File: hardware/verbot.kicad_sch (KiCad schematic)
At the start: 7 parts, among them J1 Raspberry Pi Zero 2 W, J2 5V USB power bank, M1 Pimoroni OnOff SHIM, M2 DRV8833 carrier, M3 Verbot 3V motor, M4 Verbot gearbox harness

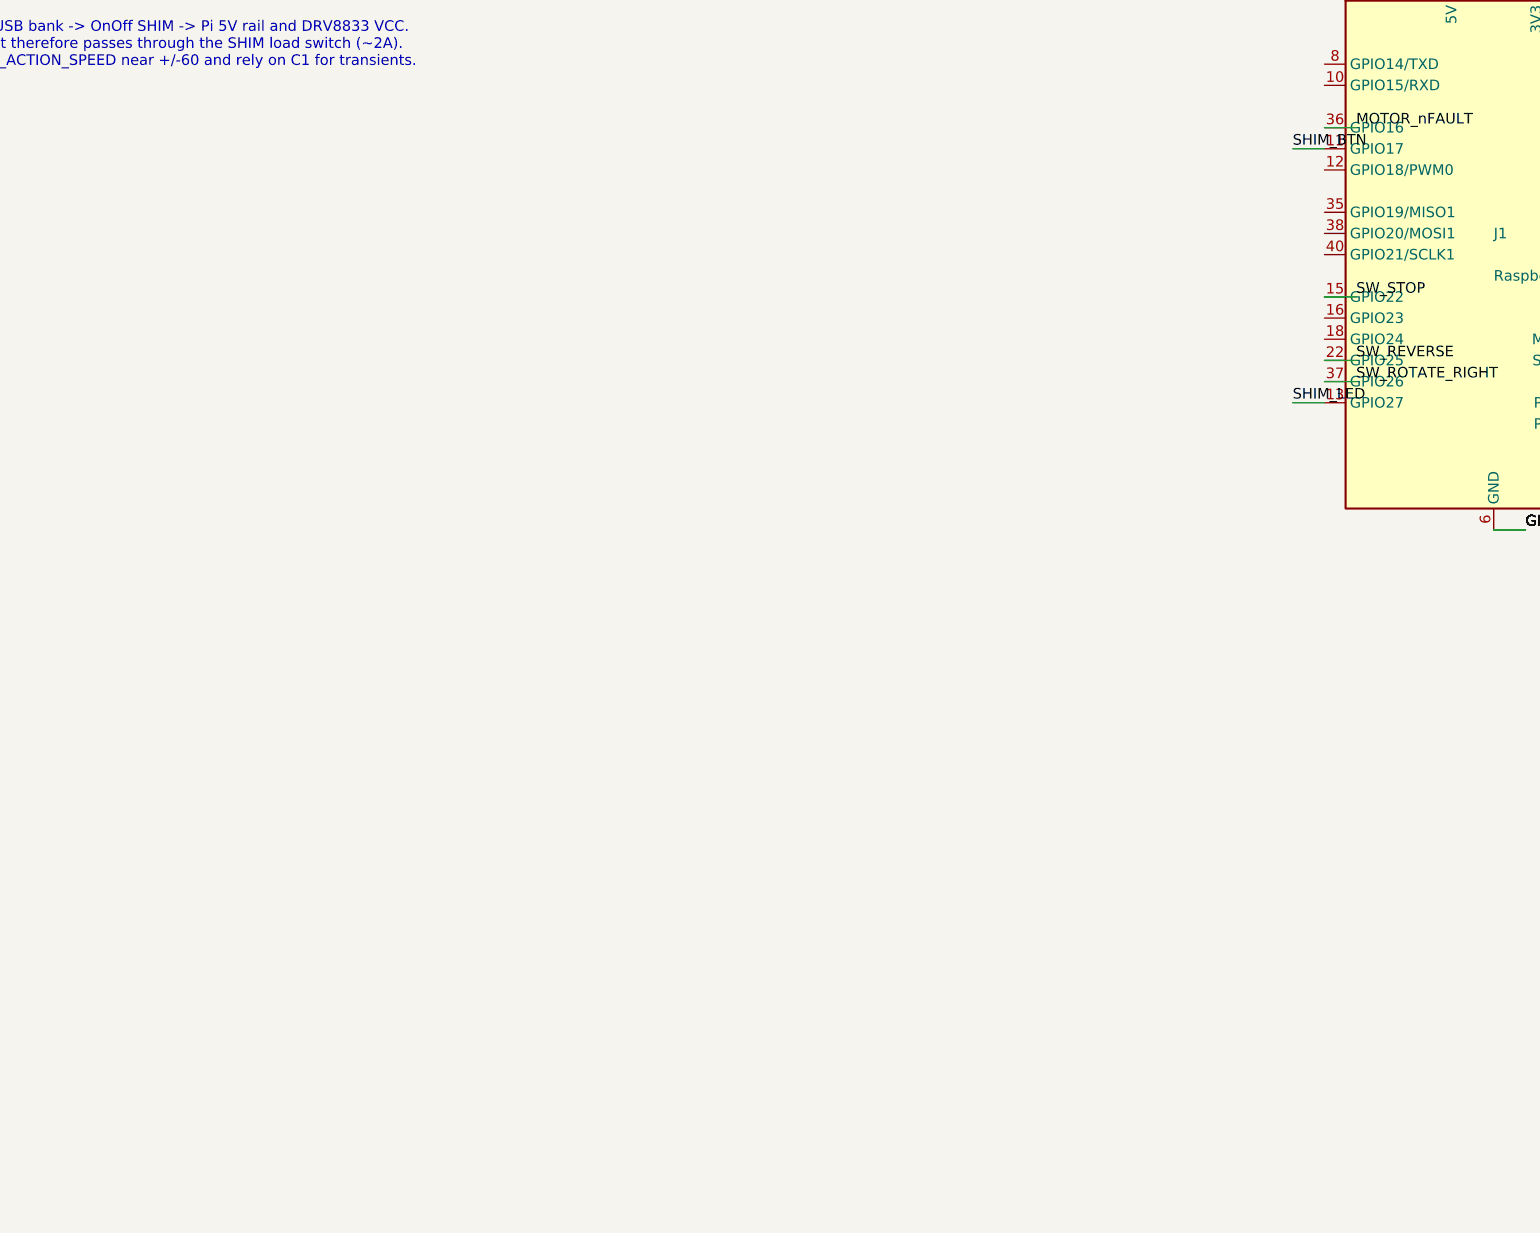
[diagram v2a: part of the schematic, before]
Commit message: feat(hardware): MAX98357A audio section
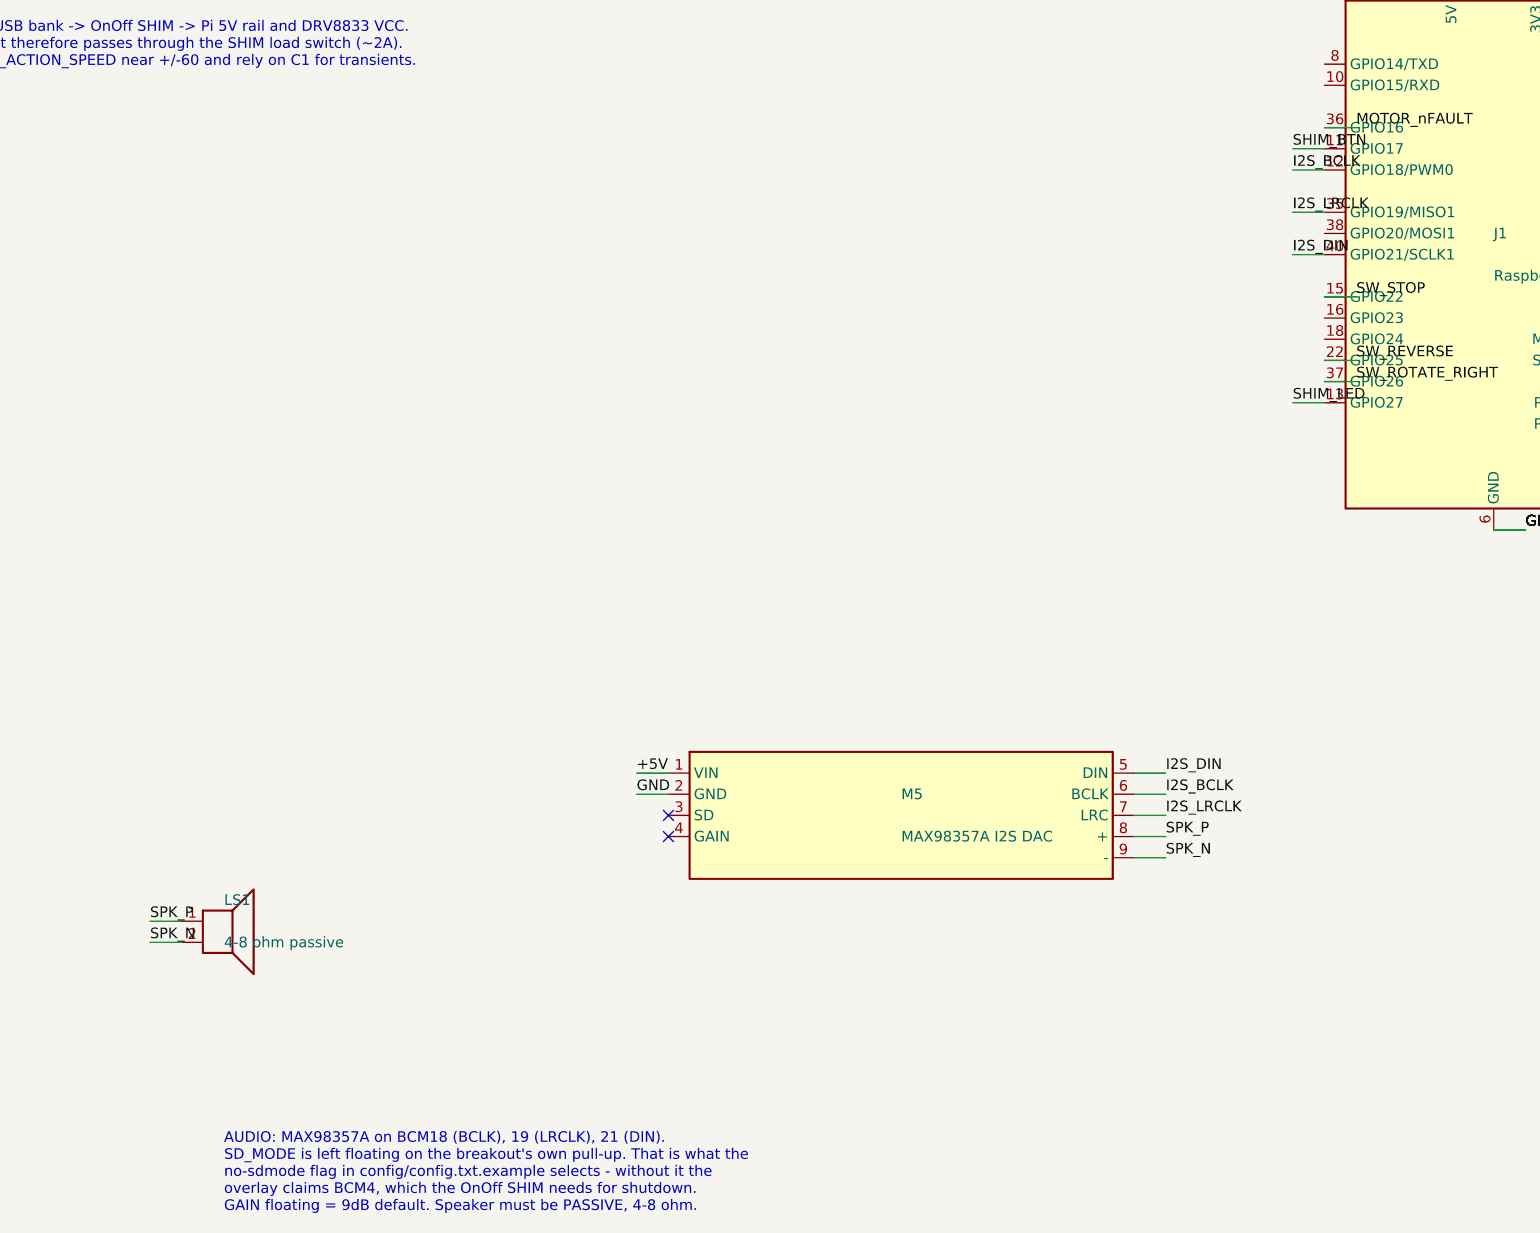
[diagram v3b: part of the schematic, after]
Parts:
- added LS1: 4-8 ohm passive, symbol Device:Speaker
- added M5: MAX98357A I2S DAC, symbol verbot:MAX98357A_Breakout
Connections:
- net +5V: now also M5.1 (VIN)
- net GND: now also M5.2 (GND)
- net I2S_BCLK: now reaches J1.12 (GPIO18/PWM0)
- net I2S_BCLK: now also M5.6 (BCLK)
- net I2S_LRCLK: now reaches J1.35 (GPIO19/MISO1)
- net I2S_LRCLK: now also M5.7 (LRC)
- net I2S_DIN: now reaches J1.40 (GPIO21/SCLK1)
- net I2S_DIN: now also M5.5 (DIN)
- new net SPK_N: LS1.2, M5.9 (-)
- new net SPK_P: LS1.1, M5.8 (+)
- no-connect marks 8 -> 10
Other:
- note added: "AUDIO: MAX98357A on BCM18 (BCLK), 19 (LRCLK), 21 (DIN). SD_MODE is left floating on the breakout's own pull-up. That is what the no-sdmode flag in config/config.txt.example selects - without it the overlay claims BCM4, which the OnOff SHIM needs for shutdown. GAIN floating = 9dB default. Speaker must be PASSIVE, 4-8 ohm."
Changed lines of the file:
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@@
 		(instances
 			(project "verbot"
-				(path "/7089de6d-abab-409e-9e27-515222eb95d8" (reference "J1") (unit 1))))
+				(path "/8c41fbdc-c236-461c-85c1-09830d1a358d" (reference "J1") (unit 1))))
 	)
 	(symbol
@@
 		(instances
 			(project "verbot"
-				(path "/7089de6d-abab-409e-9e27-515222eb95d8" (reference "M1") (unit 1))))
+				(path "/8c41fbdc-c236-461c-85c1-09830d1a358d" (reference "M1") (unit 1))))
 	)
 	(symbol
@@
 		(instances
 			(project "verbot"
-				(path "/7089de6d-abab-409e-9e27-515222eb95d8" (reference "J2") (unit 1))))
+				(path "/8c41fbdc-c236-461c-85c1-09830d1a358d" (reference "J2") (unit 1))))
 	)
 	(wire (pts (xy 26.67 58.42) (xy 30.48 58.42))
@@
 		(instances
 			(project "verbot"
-				(path "/7089de6d-abab-409e-9e27-515222eb95d8" (reference "#FLG01") (unit 1))))
+				(path "/8c41fbdc-c236-461c-85c1-09830d1a358d" (reference "#FLG01") (unit 1))))
 	)
 	(label "+5V" (at 44.45 105.41 0)
@@
 		(instances
 			(project "verbot"
-				(path "/7089de6d-abab-409e-9e27-515222eb95d8" (reference "#FLG02") (unit 1))))
+				(path "/8c41fbdc-c236-461c-85c1-09830d1a358d" (reference "#FLG02") (unit 1))))
 	)
 	(label "+3V3" (at 69.85 105.41 0)
@@
 		(instances
 			(project "verbot"
-				(path "/7089de6d-abab-409e-9e27-515222eb95d8" (reference "M2") (unit 1))))
+				(path "/8c41fbdc-c236-461c-85c1-09830d1a358d" (reference "M2") (unit 1))))
 	)
 	(symbol
@@
 		(instances
 			(project "verbot"
-				(path "/7089de6d-abab-409e-9e27-515222eb95d8" (reference "M3") (unit 1))))
+				(path "/8c41fbdc-c236-461c-85c1-09830d1a358d" (reference "M3") (unit 1))))
 	)
 	(symbol
@@
 		(instances
 			(project "verbot"
-				(path "/7089de6d-abab-409e-9e27-515222eb95d8" (reference "C1") (unit 1))))
+				(path "/8c41fbdc-c236-461c-85c1-09830d1a358d" (reference "C1") (unit 1))))
 	)
 	(wire (pts (xy 236.22 166.37) (xy 240.03 166.37))
@@
 		(instances
 			(project "verbot"
-				(path "/7089de6d-abab-409e-9e27-515222eb95d8" (reference "M4") (unit 1))))
+				(path "/8c41fbdc-c236-461c-85c1-09830d1a358d" (reference "M4") (unit 1))))
 	)
 	(wire (pts (xy 295.91 182.88) (xy 292.1 182.88))
@@
 	(text "INTERROGATION SWITCHES - all inputs, internal pull-ups, ACTIVE LOW.\nWhite is the common ground return for all eight.\n\n  colour   order  action         BCM  Pi pin\n  purple     1    stop            22    15\n  red        2    rotate right    26    37\n  yellow     3    rotate left     10    19\n  grey       4    forwards         9    21\n  blue       5    reverse         25    22\n  brown      6    put down        11    23\n  orange     7    pick up          8    24\n  green      8    talk             7    26\n\nARM LIMIT SWITCHES are in series inside the gearbox on BROWN and ORANGE.\nWhen an arm reaches its travel limit that circuit OPENS - the controller\nsees the switch release mid-action and stops. Without it the mechanism\nstrains against its stop." (at 241.3 215.9 0)
 		(effects (font (size 1.27 1.27)) (justify left top)))
+	(symbol
+		(lib_id "verbot:MAX98357A_Breakout")
+		(at 144.78 215.9 0)
+		(unit 1)
+		(exclude_from_sim no)
+		(in_bom yes)
+		(on_board yes)
+		(dnp no)
+		(property "Reference" "M5" (at 144.78 213.36 0)
+			(effects (font (size 1.27 1.27)) (justify left)))
+		(property "Value" "MAX98357A I2S DAC" (at 144.78 218.44 0)
+			(effects (font (size 1.27 1.27)) (justify left) ))
+		(pin "1")
+		(pin "2")
+		(pin "3")
+		(pin "4")
+		(pin "5")
+		(pin "6")
+		(pin "7")
+		(pin "8")
+		(pin "9")
+		(instances
+			(project "verbot"
+				(path "/8c41fbdc-c236-461c-85c1-09830d1a358d" (reference "M5") (unit 1))))
+	)
+	(symbol
+		(lib_id "Device:Speaker")
+		(at 63.5 228.6 0)
+		(unit 1)
+		(exclude_from_sim no)
+		(in_bom yes)
+		(on_board yes)
+		(dnp no)
+		(property "Reference" "LS1" (at 63.5 226.06 0)
+			(effects (font (size 1.27 1.27)) (justify left)))
+		(property "Value" "4-8 ohm passive" (at 63.5 231.14 0)
+			(effects (font (size 1.27 1.27)) (justify left) ))
+		(pin "1")
+		(pin "2")
+		(instances
+			(project "verbot"
+				(path "/8c41fbdc-c236-461c-85c1-09830d1a358d" (reference "LS1") (unit 1))))
+	)
+	(wire (pts (xy 116.84 210.82) (xy 113.03 210.82))
+		(stroke (width 0) (type default)))
+	(label "+5V" (at 113.03 210.82 0)
+		(effects (font (size 1.27 1.27)) (justify left bottom)))
+	(wire (pts (xy 116.84 213.36) (xy 113.03 213.36))
+		(stroke (width 0) (type default)))
+	(label "GND" (at 113.03 213.36 0)
+		(effects (font (size 1.27 1.27)) (justify left bottom)))
+	(wire (pts (xy 195.58 138.43) (xy 191.77 138.43))
+		(stroke (width 0) (type default)))
+	(label "I2S_BCLK" (at 191.77 138.43 0)
+		(effects (font (size 1.27 1.27)) (justify left bottom)))
+	(wire (pts (xy 172.72 213.36) (xy 176.53 213.36))
+		(stroke (width 0) (type default)))
+	(label "I2S_BCLK" (at 176.53 213.36 0)
+		(effects (font (size 1.27 1.27)) (justify left bottom)))
+	(wire (pts (xy 195.58 143.51) (xy 191.77 143.51))
+		(stroke (width 0) (type default)))
+	(label "I2S_LRCLK" (at 191.77 143.51 0)
+		(effects (font (size 1.27 1.27)) (justify left bottom)))
+	(wire (pts (xy 172.72 215.9) (xy 176.53 215.9))
+		(stroke (width 0) (type default)))
+	(label "I2S_LRCLK" (at 176.53 215.9 0)
+		(effects (font (size 1.27 1.27)) (justify left bottom)))
+	(wire (pts (xy 195.58 148.59) (xy 191.77 148.59))
+		(stroke (width 0) (type default)))
+	(label "I2S_DIN" (at 191.77 148.59 0)
+		(effects (font (size 1.27 1.27)) (justify left bottom)))
+	(wire (pts (xy 172.72 210.82) (xy 176.53 210.82))
+		(stroke (width 0) (type default)))
+	(label "I2S_DIN" (at 176.53 210.82 0)
+		(effects (font (size 1.27 1.27)) (justify left bottom)))
+	(no_connect (at 116.84 215.9))
+	(no_connect (at 116.84 218.44))
+	(wire (pts (xy 172.72 218.44) (xy 176.53 218.44))
+		(stroke (width 0) (type default)))
+	(label "SPK_P" (at 176.53 218.44 0)
+		(effects (font (size 1.27 1.27)) (justify left bottom)))
+	(wire (pts (xy 172.72 220.98) (xy 176.53 220.98))
+		(stroke (width 0) (type default)))
+	(label "SPK_N" (at 176.53 220.98 0)
+		(effects (font (size 1.27 1.27)) (justify left bottom)))
+	(wire (pts (xy 58.42 228.6) (xy 54.61 228.6))
+		(stroke (width 0) (type default)))
+	(label "SPK_P" (at 54.61 228.6 0)
+		(effects (font (size 1.27 1.27)) (justify left bottom)))
+	(wire (pts (xy 58.42 231.14) (xy 54.61 231.14))
+		(stroke (width 0) (type default)))
+	(label "SPK_N" (at 54.61 231.14 0)
+		(effects (font (size 1.27 1.27)) (justify left bottom)))
+	(text "AUDIO: MAX98357A on BCM18 (BCLK), 19 (LRCLK), 21 (DIN).\nSD_MODE is left floating on the breakout's own pull-up. That is what the\nno-sdmode flag in config/config.txt.example selects - without it the\noverlay claims BCM4, which the OnOff SHIM needs for shutdown.\nGAIN floating = 9dB default. Speaker must be PASSIVE, 4-8 ohm." (at 63.5 254.0 0)
+		(effects (font (size 1.27 1.27)) (justify left top)))
 	(sheet_instances
